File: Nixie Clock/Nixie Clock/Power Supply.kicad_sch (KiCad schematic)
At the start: 17 parts, among them Q1 MPSA55, U1 MC34063AP

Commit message: More Nixie Stuff
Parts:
- added C?: 10uF, symbol Device:C_Polarized
- added C?: 10 uF tantalum, symbol Device:C_Polarized
- added J1: PJ-202A, digikey-footprints:Barrel_Jack_5.5mmODx2.1mmID_PJ-202A, symbol dk_Barrel-Power-Connectors:PJ-202A
- added U1: LM1086IT-5.0, TO254P1054X470X1955-3, symbol LM1086IT-5.0:LM1086IT-5.0
- gave numbers to parts that had none: 1
- renumbered C6 to C1, C4 to C2, C1 to C3, C2 to C4, R5 to R1, R6 to R2, R4 to R3, R2 to R4, R3 to R5, R7 to R6, R1 to R7, U1 to U2
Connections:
- net +12V: now also C?.1, J1.1, U1.3 (VIN)
- net GND: now also C?.2, C?.2, J1.2, J1.3, U1.1 (ADJ/GND)
- new net +5V: C?.1, U1.2 (VOUT)
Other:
- moved on the sheet: C1, C2, C3, C4, D1, D2, L1, Q1, R1, R2, R3, R4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

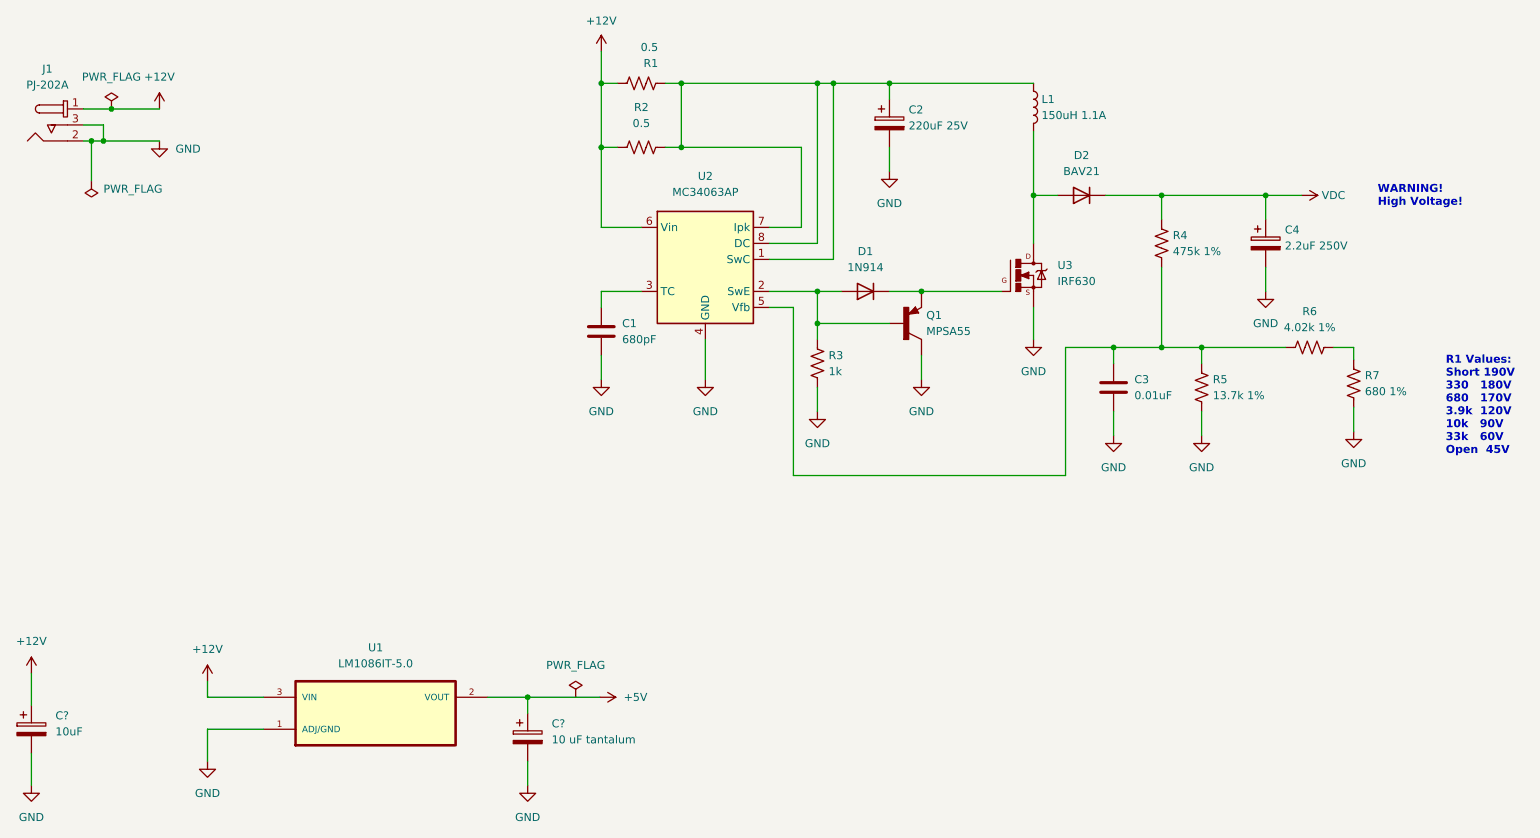
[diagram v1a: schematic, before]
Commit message: Need to add footprints for passives
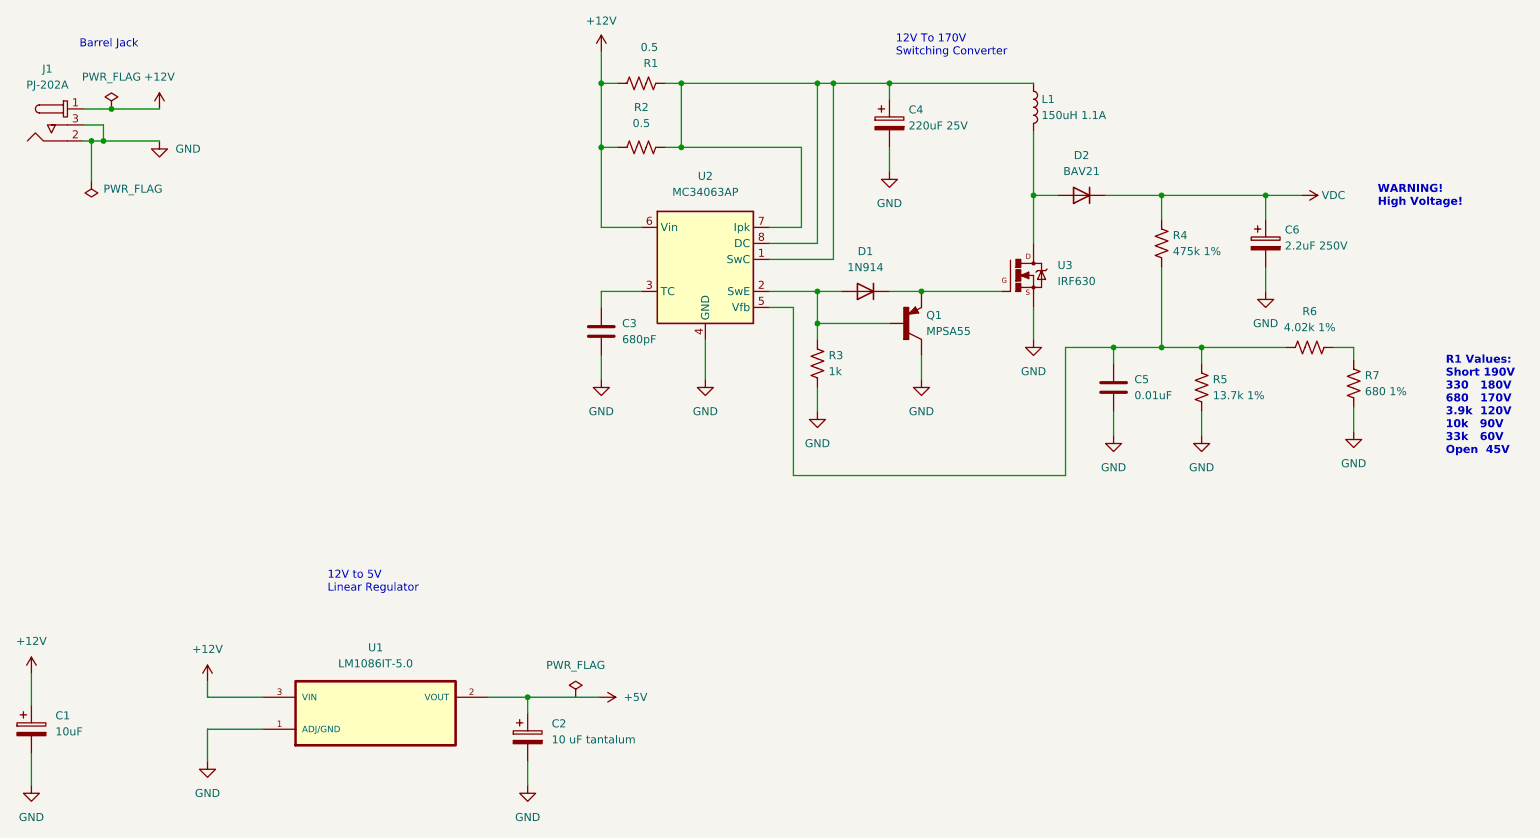
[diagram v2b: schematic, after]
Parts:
- Q1: footprint TO92127P520H787-3 -> MPSA55:TO92127P520H787-3
- U1: footprint TO254P1054X470X1955-3 -> LM1086IT-5:TO254P1054X470X1955-3
- U3: footprint TO220V -> IRF630:TO220V
- gave numbers to parts that had none: 2
- renumbered C1 to C3, C2 to C4, C3 to C5, C4 to C6
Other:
- note added: "12V To 170V Switching Converter"
- note added: "12V to 5V Linear Regulator"
- note added: "Barrel Jack"
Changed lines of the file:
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@@
     (stroke (width 0) (type default) (color 0 0 0 0))
+  )
+  (text "Barrel Jack" (at 36.83 31.75 0)
+    (effects (font (size 1.27 1.27)) (justify left bottom))
   )
   (text "R1 Values: \nShort 190V\n330   180V\n680   170V\n3.9k  120V\n10k   90V\n33k   60V\nOpen  45V"
@@
     (effects (font (size 1.27 1.27) bold) (justify left bottom))
   )
+  (text "12V to 5V\nLinear Regulator" (at 76.2 118.11 0)
+    (effects (font (size 1.27 1.27)) (justify left bottom))
+  )
+  (text "12V To 170V \nSwitching Converter\n" (at 166.37 33.02 0)
+    (effects (font (size 1.27 1.27)) (justify left bottom))
+  )
   (text "WARNING! \nHigh Voltage!" (at 242.824 56.896 0)
     (effects (font (size 1.27 1.27) (thickness 0.254) bold) (justify left bottom))
@@
     (property "Reference" "U1" (id 0) (at 83.82 126.746 0))
     (property "Value" "LM1086IT-5.0" (id 1) (at 83.82 129.286 0))
-    (property "Footprint" "TO254P1054X470X1955-3" (id 2) (at 83.82 137.16 0)
+    (property "Footprint" "LM1086IT-5:TO254P1054X470X1955-3" (id 2) (at 83.82 137.16 0)
       (effects (font (size 1.27 1.27)) (justify left bottom) hide)
     )
@@
   (symbol (lib_id "power:+12V") (at 49.53 41.275 0) (unit 1)
     (in_bom yes) (on_board yes) (fields_autoplaced)
-    (property "Reference" "#PWR01" (id 0) (at 49.53 45.085 0)
+    (property "Reference" "#PWR03" (id 0) (at 49.53 45.085 0)
       (effects (font (size 1.27 1.27)) hide)
     )
@@
   (symbol (lib_id "power:GND") (at 153.924 89.281 0) (unit 1)
     (in_bom yes) (on_board yes) (fields_autoplaced)
-    (property "Reference" "#PWR06" (id 0) (at 153.924 95.631 0)
+    (property "Reference" "#PWR012" (id 0) (at 153.924 95.631 0)
       (effects (font (size 1.27 1.27)) hide)
     )
@@
   (symbol (lib_id "power:+5V") (at 119.38 134.62 270) (unit 1)
     (in_bom yes) (on_board yes) (fields_autoplaced)
-    (property "Reference" "#PWR?" (id 0) (at 115.57 134.62 0)
+    (property "Reference" "#PWR08" (id 0) (at 115.57 134.62 0)
       (effects (font (size 1.27 1.27)) hide)
     )
@@
   (symbol (lib_id "power:GND") (at 49.53 46.355 0) (unit 1)
     (in_bom yes) (on_board yes) (fields_autoplaced)
-    (property "Reference" "#PWR02" (id 0) (at 49.53 52.705 0)
+    (property "Reference" "#PWR04" (id 0) (at 49.53 52.705 0)
       (effects (font (size 1.27 1.27)) hide)
     )
@@
   (symbol (lib_id "power:+12V") (at 57.15 132.08 0) (unit 1)
     (in_bom yes) (on_board yes) (fields_autoplaced)
-    (property "Reference" "#PWR?" (id 0) (at 57.15 135.89 0)
+    (property "Reference" "#PWR05" (id 0) (at 57.15 135.89 0)
       (effects (font (size 1.27 1.27)) hide)
     )
@@
   (symbol (lib_id "Device:C_Polarized") (at 29.21 139.7 0) (unit 1)
     (in_bom yes) (on_board yes) (fields_autoplaced)
-    (property "Reference" "C?" (id 0) (at 33.02 137.5409 0)
+    (property "Reference" "C1" (id 0) (at 33.02 137.5409 0)
       (effects (font (size 1.27 1.27)) (justify left))
     )
@@
   (symbol (lib_id "power:GND") (at 165.354 51.181 0) (unit 1)
     (in_bom yes) (on_board yes) (fields_autoplaced)
-    (property "Reference" "#PWR07" (id 0) (at 165.354 57.531 0)
+    (property "Reference" "#PWR013" (id 0) (at 165.354 57.531 0)
       (effects (font (size 1.27 1.27)) hide)
     )
@@
   (symbol (lib_id "power:GND") (at 225.044 70.231 0) (unit 1)
     (in_bom yes) (on_board yes) (fields_autoplaced)
-    (property "Reference" "#PWR012" (id 0) (at 225.044 76.581 0)
+    (property "Reference" "#PWR018" (id 0) (at 225.044 76.581 0)
       (effects (font (size 1.27 1.27)) hide)
     )
@@
   (symbol (lib_id "power:GND") (at 239.014 92.456 0) (unit 1)
     (in_bom yes) (on_board yes) (fields_autoplaced)
-    (property "Reference" "#PWR014" (id 0) (at 239.014 98.806 0)
+    (property "Reference" "#PWR020" (id 0) (at 239.014 98.806 0)
       (effects (font (size 1.27 1.27)) hide)
     )
@@
   (symbol (lib_id "power:GND") (at 119.634 84.201 0) (unit 1)
     (in_bom yes) (on_board yes) (fields_autoplaced)
-    (property "Reference" "#PWR04" (id 0) (at 119.634 90.551 0)
+    (property "Reference" "#PWR010" (id 0) (at 119.634 90.551 0)
       (effects (font (size 1.27 1.27)) hide)
     )
@@
   (symbol (lib_id "power:GND") (at 214.884 93.091 0) (unit 1)
     (in_bom yes) (on_board yes) (fields_autoplaced)
-    (property "Reference" "#PWR011" (id 0) (at 214.884 99.441 0)
+    (property "Reference" "#PWR017" (id 0) (at 214.884 99.441 0)
       (effects (font (size 1.27 1.27)) hide)
     )
@@
   (symbol (lib_id "power:+12V") (at 119.634 32.131 0) (unit 1)
     (in_bom yes) (on_board yes) (fields_autoplaced)
-    (property "Reference" "#PWR03" (id 0) (at 119.634 35.941 0)
+    (property "Reference" "#PWR09" (id 0) (at 119.634 35.941 0)
       (effects (font (size 1.27 1.27)) hide)
     )
@@
   (symbol (lib_id "Device:C") (at 200.914 85.471 0) (unit 1)
     (in_bom yes) (on_board yes) (fields_autoplaced)
-    (property "Reference" "C3" (id 0) (at 204.216 84.2009 0)
+    (property "Reference" "C5" (id 0) (at 204.216 84.2009 0)
       (effects (font (size 1.27 1.27)) (justify left))
     )
@@
   (symbol (lib_id "Device:C_Polarized") (at 165.354 43.561 0) (unit 1)
     (in_bom yes) (on_board yes) (fields_autoplaced)
-    (property "Reference" "C2" (id 0) (at 168.402 41.4019 0)
+    (property "Reference" "C4" (id 0) (at 168.402 41.4019 0)
       (effects (font (size 1.27 1.27)) (justify left))
     )
@@
       (effects (font (size 1.27 1.27)) (justify left))
     )
-    (property "Footprint" "TO220V" (id 2) (at 185.674 67.691 0)
+    (property "Footprint" "IRF630:TO220V" (id 2) (at 185.674 67.691 0)
       (effects (font (size 1.27 1.27)) (justify left bottom) hide)
     )
@@
   (symbol (lib_id "power:+12V") (at 29.21 130.81 0) (unit 1)
     (in_bom yes) (on_board yes) (fields_autoplaced)
-    (property "Reference" "#PWR?" (id 0) (at 29.21 134.62 0)
+    (property "Reference" "#PWR01" (id 0) (at 29.21 134.62 0)
       (effects (font (size 1.27 1.27)) hide)
     )
@@
   (symbol (lib_id "power:PWR_FLAG") (at 115.57 134.62 0) (unit 1)
     (in_bom yes) (on_board yes) (fields_autoplaced)
-    (property "Reference" "#FLG?" (id 0) (at 115.57 132.715 0)
+    (property "Reference" "#FLG03" (id 0) (at 115.57 132.715 0)
       (effects (font (size 1.27 1.27)) hide)
     )
@@
   (symbol (lib_id "power:GND") (at 29.21 148.59 0) (unit 1)
     (in_bom yes) (on_board yes) (fields_autoplaced)
-    (property "Reference" "#PWR?" (id 0) (at 29.21 154.94 0)
+    (property "Reference" "#PWR02" (id 0) (at 29.21 154.94 0)
       (effects (font (size 1.27 1.27)) hide)
     )
@@
   (symbol (lib_id "power:GND") (at 57.15 144.78 0) (unit 1)
     (in_bom yes) (on_board yes) (fields_autoplaced)
-    (property "Reference" "#PWR?" (id 0) (at 57.15 151.13 0)
+    (property "Reference" "#PWR06" (id 0) (at 57.15 151.13 0)
       (effects (font (size 1.27 1.27)) hide)
     )
@@
       (effects (font (size 1.27 1.27)) (justify left))
     )
-    (property "Footprint" "TO92127P520H787-3" (id 2) (at 167.894 75.311 0)
+    (property "Footprint" "MPSA55:TO92127P520H787-3" (id 2) (at 167.894 75.311 0)
       (effects (font (size 1.27 1.27)) (justify left bottom) hide)
     )
@@
   (symbol (lib_id "power:GND") (at 170.434 84.201 0) (unit 1)
     (in_bom yes) (on_board yes) (fields_autoplaced)
-    (property "Reference" "#PWR08" (id 0) (at 170.434 90.551 0)
+    (property "Reference" "#PWR014" (id 0) (at 170.434 90.551 0)
       (effects (font (size 1.27 1.27)) hide)
     )
@@
   (symbol (lib_id "power:GND") (at 107.95 148.59 0) (unit 1)
     (in_bom yes) (on_board yes) (fields_autoplaced)
-    (property "Reference" "#PWR?" (id 0) (at 107.95 154.94 0)
+    (property "Reference" "#PWR07" (id 0) (at 107.95 154.94 0)
       (effects (font (size 1.27 1.27)) hide)
     )
@@
   (symbol (lib_id "power:GND") (at 188.214 77.851 0) (unit 1)
     (in_bom yes) (on_board yes) (fields_autoplaced)
-    (property "Reference" "#PWR09" (id 0) (at 188.214 84.201 0)
+    (property "Reference" "#PWR015" (id 0) (at 188.214 84.201 0)
       (effects (font (size 1.27 1.27)) hide)
     )
@@
   (symbol (lib_id "Device:C") (at 119.634 76.581 0) (unit 1)
     (in_bom yes) (on_board yes) (fields_autoplaced)
-    (property "Reference" "C1" (id 0) (at 122.936 75.3109 0)
+    (property "Reference" "C3" (id 0) (at 122.936 75.3109 0)
       (effects (font (size 1.27 1.27)) (justify left))
     )
@@
   (symbol (lib_id "power:GND") (at 136.144 84.201 0) (unit 1)
     (in_bom yes) (on_board yes) (fields_autoplaced)
-    (property "Reference" "#PWR05" (id 0) (at 136.144 90.551 0)
+    (property "Reference" "#PWR011" (id 0) (at 136.144 90.551 0)
       (effects (font (size 1.27 1.27)) hide)
     )
@@
   (symbol (lib_id "power:VDC") (at 230.759 54.991 270) (unit 1)
     (in_bom yes) (on_board yes) (fields_autoplaced)
-    (property "Reference" "#PWR013" (id 0) (at 228.219 54.991 0)
+    (property "Reference" "#PWR019" (id 0) (at 228.219 54.991 0)
       (effects (font (size 1.27 1.27)) hide)
     )
@@
   (symbol (lib_id "Device:C_Polarized") (at 107.95 140.97 0) (unit 1)
     (in_bom yes) (on_board yes) (fields_autoplaced)
-    (property "Reference" "C?" (id 0) (at 111.76 138.8109 0)
+    (property "Reference" "C2" (id 0) (at 111.76 138.8109 0)
       (effects (font (size 1.27 1.27)) (justify left))
     )
@@
   (symbol (lib_id "power:GND") (at 200.914 93.091 0) (unit 1)
     (in_bom yes) (on_board yes) (fields_autoplaced)
-    (property "Reference" "#PWR010" (id 0) (at 200.914 99.441 0)
+    (property "Reference" "#PWR016" (id 0) (at 200.914 99.441 0)
       (effects (font (size 1.27 1.27)) hide)
     )
@@
   (symbol (lib_id "Device:C_Polarized") (at 225.044 62.611 0) (unit 1)
     (in_bom yes) (on_board yes) (fields_autoplaced)
-    (property "Reference" "C4" (id 0) (at 228.092 60.4519 0)
-      (effects (font (size 1.27 1.27)) (justify left))
-    )
+    (property "Reference" "C6" (id 0) (at 228.092 60.4519 0)
+      (effects (font (size 1.27 1.27)) (justify left))
+    )

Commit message: Started Routing
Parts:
- C1: footprint (none) -> Capacitor_THT:CP_Radial_D5.0mm_P2.00mm
- C2: value 10 uF tantalum -> 10 uF; footprint (none) -> Capacitor_THT:CP_Radial_D5.0mm_P2.00mm
- C3: footprint (none) -> Capacitor_THT:C_Disc_D7.5mm_W4.4mm_P5.00mm
- C4: footprint (none) -> Capacitor_THT:CP_Radial_D10.0mm_P5.00mm
- C5: footprint (none) -> Capacitor_THT:C_Disc_D12.0mm_W4.4mm_P7.75mm
- C6: footprint (none) -> Capacitor_THT:CP_Radial_D6.3mm_P2.50mm
- L1: footprint (none) -> Inductor_THT:L_Radial_D12.0mm_P10.00mm_Neosid_SD12_style1
- R1, R2, R3, R4, R5, R6, R7: footprint (none) -> Resistor_THT:R_Axial_DIN0207_L6.3mm_D2.5mm_P10.16mm_Horizontal
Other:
- note added: "R7 Values: Short 190V 330 180V 680 170V 3.9k 120V 10k 90V 33k 60V Open 45V"
- note removed: "R1 Values: Short 190V 330 180V 680 170V 3.9k 120V 10k 90V 33k 60V Open 45V"
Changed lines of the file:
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@@
     (effects (font (size 1.27 1.27)) (justify left bottom))
   )
-  (text "R1 Values: \nShort 190V\n330   180V\n680   170V\n3.9k  120V\n10k   90V\n33k   60V\nOpen  45V"
+  (text "R7 Values: \nShort 190V\n330   180V\n680   170V\n3.9k  120V\n10k   90V\n33k   60V\nOpen  45V"
     (at 253.619 96.266 0)
     (effects (font (size 1.27 1.27) bold) (justify left bottom))
@@
     (property "Reference" "R2" (id 0) (at 125.984 41.021 90))
     (property "Value" "0.5" (id 1) (at 125.984 43.561 90))
-    (property "Footprint" "" (id 2) (at 126.238 46.355 90)
+    (property "Footprint" "Resistor_THT:R_Axial_DIN0207_L6.3mm_D2.5mm_P10.16mm_Horizontal" (id 2) (at 126.238 46.355 90)
       (effects (font (size 1.27 1.27)) hide)
     )
@@
       (effects (font (size 1.27 1.27)) (justify left))
     )
-    (property "Footprint" "" (id 2) (at 188.214 41.021 0)
+    (property "Footprint" "Inductor_THT:L_Radial_D12.0mm_P10.00mm_Neosid_SD12_style1" (id 2) (at 188.214 41.021 0)
       (effects (font (size 1.27 1.27)) hide)
     )
@@
       (effects (font (size 1.27 1.27)) (justify left))
     )
-    (property "Footprint" "" (id 2) (at 126.238 36.195 90)
+    (property "Footprint" "Resistor_THT:R_Axial_DIN0207_L6.3mm_D2.5mm_P10.16mm_Horizontal" (id 2) (at 126.238 36.195 90)
       (effects (font (size 1.27 1.27)) hide)
     )
@@
       (effects (font (size 1.27 1.27)) (justify left))
     )
-    (property "Footprint" "" (id 2) (at 30.1752 143.51 0)
+    (property "Footprint" "Capacitor_THT:CP_Radial_D5.0mm_P2.00mm" (id 2) (at 30.1752 143.51 0)
       (effects (font (size 1.27 1.27)) hide)
     )
@@
       (effects (font (size 1.27 1.27)) (justify left))
     )
-    (property "Footprint" "" (id 2) (at 154.94 81.915 90)
+    (property "Footprint" "Resistor_THT:R_Axial_DIN0207_L6.3mm_D2.5mm_P10.16mm_Horizontal" (id 2) (at 154.94 81.915 90)
       (effects (font (size 1.27 1.27)) hide)
     )
@@
       (effects (font (size 1.27 1.27)) (justify left))
     )
-    (property "Footprint" "" (id 2) (at 209.55 62.865 90)
+    (property "Footprint" "Resistor_THT:R_Axial_DIN0207_L6.3mm_D2.5mm_P10.16mm_Horizontal" (id 2) (at 209.55 62.865 90)
       (effects (font (size 1.27 1.27)) hide)
     )
@@
       (effects (font (size 1.27 1.27)) (justify left))
     )
-    (property "Footprint" "" (id 2) (at 201.8792 89.281 0)
+    (property "Footprint" "Capacitor_THT:C_Disc_D12.0mm_W4.4mm_P7.75mm" (id 2) (at 201.8792 89.281 0)
       (effects (font (size 1.27 1.27)) hide)
     )
@@
       (effects (font (size 1.27 1.27)) (justify left))
     )
-    (property "Footprint" "" (id 2) (at 166.3192 47.371 0)
+    (property "Footprint" "Capacitor_THT:CP_Radial_D10.0mm_P5.00mm" (id 2) (at 166.3192 47.371 0)
       (effects (font (size 1.27 1.27)) hide)
     )
@@
     (property "Reference" "R6" (id 0) (at 232.029 73.406 90))
     (property "Value" "4.02k 1%" (id 1) (at 232.029 75.946 90))
-    (property "Footprint" "" (id 2) (at 231.775 80.137 90)
+    (property "Footprint" "Resistor_THT:R_Axial_DIN0207_L6.3mm_D2.5mm_P10.16mm_Horizontal" (id 2) (at 231.775 80.137 90)
       (effects (font (size 1.27 1.27)) hide)
     )
@@
       (effects (font (size 1.27 1.27)) (justify left))
     )
-    (property "Footprint" "" (id 2) (at 215.9 85.725 90)
+    (property "Footprint" "Resistor_THT:R_Axial_DIN0207_L6.3mm_D2.5mm_P10.16mm_Horizontal" (id 2) (at 215.9 85.725 90)
       (effects (font (size 1.27 1.27)) hide)
     )
@@
       (effects (font (size 1.27 1.27)) (justify left))
     )
-    (property "Footprint" "" (id 2) (at 240.03 85.09 90)
+    (property "Footprint" "Resistor_THT:R_Axial_DIN0207_L6.3mm_D2.5mm_P10.16mm_Horizontal" (id 2) (at 240.03 85.09 90)
       (effects (font (size 1.27 1.27)) hide)
     )
@@
       (effects (font (size 1.27 1.27)) (justify left))
     )
-    (property "Footprint" "" (id 2) (at 120.5992 80.391 0)
+    (property "Footprint" "Capacitor_THT:C_Disc_D7.5mm_W4.4mm_P5.00mm" (id 2) (at 120.5992 80.391 0)
       (effects (font (size 1.27 1.27)) hide)
     )
@@
       (effects (font (size 1.27 1.27)) (justify left))
     )
-    (property "Value" "10 uF tantalum" (id 1) (at 111.76 141.3509 0)
-      (effects (font (size 1.27 1.27)) (justify left))
-    )
-    (property "Footprint" "" (id 2) (at 108.9152 144.78 0)
+    (property "Value" "10 uF " (id 1) (at 111.76 141.3509 0)
+      (effects (font (size 1.27 1.27)) (justify left))
+    )
+    (property "Footprint" "Capacitor_THT:CP_Radial_D5.0mm_P2.00mm" (id 2) (at 108.9152 144.78 0)
       (effects (font (size 1.27 1.27)) hide)
     )
@@
       (effects (font (size 1.27 1.27)) (justify left))
     )
-    (property "Footprint" "" (id 2) (at 226.0092 66.421 0)
-      (effects (font (size 1.27 1.27)) hide)
-    )
+    (property "Footprint" "Capacitor_THT:CP_Radial_D6.3mm_P2.50mm" (id 2) (at 226.0092 66.421 0)
+      (effects (font (size 1.27 1.27)) hide)
+    )
